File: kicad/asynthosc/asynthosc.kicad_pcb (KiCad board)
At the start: 4 copper layers, 71.5 x 128.5 mm, 201 parts, among them J1 USB_B_Micro, J11 Conn_01x04_Pin, J13 AudioJack3, J14 AudioJack3, J15 AudioJack3, J16 AudioJack3, J2 Conn_02x05_Odd_Even, J4 AudioJack3, J5 AudioJack3, J6 Conn_01x04_Pin, J7 AudioJack3, J9 Conn_01x07_Pin, Q2 Q_NPN_BEC, SW4 SW_MEC_5G_LED, SW7 SW_MEC_5G_LED, U1 LM1117S-3.3, U10 W25Q32JVSS, U11 LM1117S-5.0, U12 Si1869DH, U2 STM32H723ZGTx, U3 MCP6004, U4 MCP6004, U5 LAN8742A, U6 USBLC6-2P6, U7 USBLC6-2SC6, U8 H11L1, U9 LMR62421XMF, Y1 8MHz, 8pF, Y2 25MHZ,20PF,30PPM

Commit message: wip
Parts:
- removed the J13 at (103.5, 82.0)
- removed the J13 at (115.0, 82.0)
- removed the J13 at (126.5, 106.0)
- removed the J13 at (138.0, 106.0)
- removed the J13 at (115.0, 106.0)
- removed J6: Conn_01x04_Pin, Connector_PinHeader_2.54mm:PinHeader_1x04_P2.54mm_Vertical
- removed the SW4 at (116.5, 70.5)
- removed the SW4 at (107.5, 70.5)
- removed the SW4 at (134.5, 70.5)
- removed the SW4 at (138.0, 96.0)
- removed the SW4 at (114.5, 96.0)
- removed the SW4 at (126.5, 96.0)
- removed the SW4 at (125.5, 70.5)
- added C46: 10u, Capacitor_SMD:CP_Elec_4x5.4, F.Cu at (267.4, 47.4)
- added C55: 100n, Capacitor_SMD:C_0402_1005Metric, F.Cu at (258.7, 48.3)
- added C56: 100n, Capacitor_SMD:C_0402_1005Metric, F.Cu at (258.7, 50.2)
- added C57: 100n, Capacitor_SMD:C_0603_1608Metric, F.Cu at (227.2, 110.5)
- added F1: Fuse, 1.25A, trip 2.5A, Resistor_SMD:R_0805_2012Metric, F.Cu at (265.7, 51.8)
- added FB1: BLM15PX330SN1D, Inductor_SMD:L_0402_1005Metric, F.Cu at (269.4, 51.3)
- added FB2: BLM15PX330SN1D, Inductor_SMD:L_0402_1005Metric, F.Cu at (265.0, 41.5)
- added FB3: BLM15PX330SN1D, Inductor_SMD:L_0402_1005Metric, F.Cu at (265.0, 56.3)
- added J10: Conn_02x07_Odd_Even, Connector_PinSocket_2.54mm:PinSocket_2x07_P2.54mm_Vertical_SMD, B.Cu at (121.0, 138.1)
- added J12: Conn_02x04_Odd_Even, Connector_PinHeader_2.54mm:PinHeader_2x04_P2.54mm_Vertical_SMD, B.Cu at (140.5, 142.2)
- added J3: RJ45_LED_Shielded, asynthosc:RJ45_HCTL_HC-RJ45-053-2, F.Cu at (139.4, 51.8)
- added J8: AudioJack3, asynthosc:Jack_3.5mm_3legs_XKB_PJ-3411_Vertical, F.Cu at (104.5, 84.7)
- added J9: Conn_ARM_SWD_TagConnect_TC2030-NL, Connector:Tag-Connect_TC2030-IDC-NL_2x03_P1.27mm_Vertical, F.Cu at (151.0, 147.5)
- added Q1: Q_NPN_BEC, Package_TO_SOT_SMD:SOT-23, F.Cu at (242.6, 107.5)
- added R75: 10k, Resistor_SMD:R_0402_1005Metric, F.Cu at (255.8, 48.3)
- added R77: 10k, Resistor_SMD:R_0402_1005Metric, F.Cu at (255.8, 50.3)
- added R78: 10k, Resistor_SMD:R_0402_1005Metric, F.Cu at (255.8, 52.2)
- added R79: 270R, Resistor_SMD:R_0402_1005Metric, F.Cu at (255.8, 54.2)
- added R80: 100k, Resistor_SMD:R_0402_1005Metric, F.Cu at (238.7, 106.1)
- added R81: 10k, Resistor_SMD:R_0402_1005Metric, F.Cu at (238.7, 108.1)
- added R82: 270R, Resistor_SMD:R_0402_1005Metric, F.Cu at (238.7, 110.1)
- added REF**: LQFP-100_14x14mm_P0.5mm, Package_QFP:LQFP-100_14x14mm_P0.5mm, F.Cu at (145.0, 131.5)
- added SW10: SW_MEC_5G_LED, asynthosc:TPB01-X0XLXX_SW_MEC_5G, F.Cu at (136.0, 108.5)
- added SW2: SW_Push, Button_Switch_SMD:SW_SPST_B3S-1000, B.Cu at (97.2, 144.2)
- added SW3: RotaryEncoder, Rotary_Encoder:RotaryEncoder_Alps_EC12E_Vertical_H20mm, F.Cu at (118.0, 80.5)
- added SW9: SW_MEC_5G_LED, asynthosc:TPB01-X0XLXX_SW_MEC_5G, F.Cu at (134.0, 72.0)
- added TH1: Thermistor_NTC, Resistor_THT:R_Axial_DIN0204_L3.6mm_D1.6mm_P7.62mm_Horizontal, F.Cu at (168.0, 44.0)
- Q2: footprint Resistor_SMD:R_0402_1005Metric -> Package_TO_SOT_SMD:SOT-23
- moved D2 175.3 mm to (51.5, 43.6)
- moved U12 170.6 mm to (51.8, 49.7)
- moved U11 126.7 mm to (67.7, 47.6)
- moved J7 117.7 mm to (115.0, 86.8)
- moved Y1 106.7 mm to (106.5, 134.0)
- moved Y2 99.3 mm to (96.5, 121.5)
- moved J16 96.9 mm to (137.2, 97.0), turned to 90 degrees
- moved J14 94.6 mm to (104.0, 95.8), turned to -90 degrees
- moved U10 74.0 mm to (101.6, 142.6)
- moved SW7 71.3 mm to (107.5, 72.0)
- moved L1 59.6 mm to (88.0, 84.5)
- moved J15 55.0 mm to (125.8, 99.0)
- moved TR1 41.5 mm to (146.8, 67.2)
- moved U1 27.9 mm to (102.4, 60.5)
- moved R76 27.6 mm to (183.5, 43.5)
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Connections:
- R15 pad 1: Net-(J9-Pin_4) -> /Soc/JTMS_CONN
- R16 pad 1: Net-(J9-Pin_5) -> /Soc/NRST_CONN
- R17 pad 1: Net-(J9-Pin_6) -> /Soc/JTDO_CONN
- R20 pad 1: Net-(J11-Pin_1) -> Net-(J12-Pin_7)
- R7 pad 1: Net-(J9-Pin_7) -> /Soc/JTDI_CONN
- R8 pad 1: Net-(J9-Pin_2) -> /Soc/JTCK_CONN
- U2 pad 66: /Soc/TIM1_CH3 -> /Analog_in/TRG1
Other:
- board size 71.5 x 128.5 mm -> 69 x 106 mm
- board text added: "(OK)"
- board text added: "(cancel)"
- board text added: "13mm between boards"
- board text added: "71.12 mm = 14 x 5.08mm = 14 HP"
- board text added: "AUDIO OUT"
- board text added: "BTN"
- board text added: "CV"
- board text added: "DISPLAY"
- board text added: "JACK"
- board text added: "MIDI IN"
- board text added: "PANEL"
- board text added: "PCB"
- board text added: "ROT"
- board text added: "TRIG"

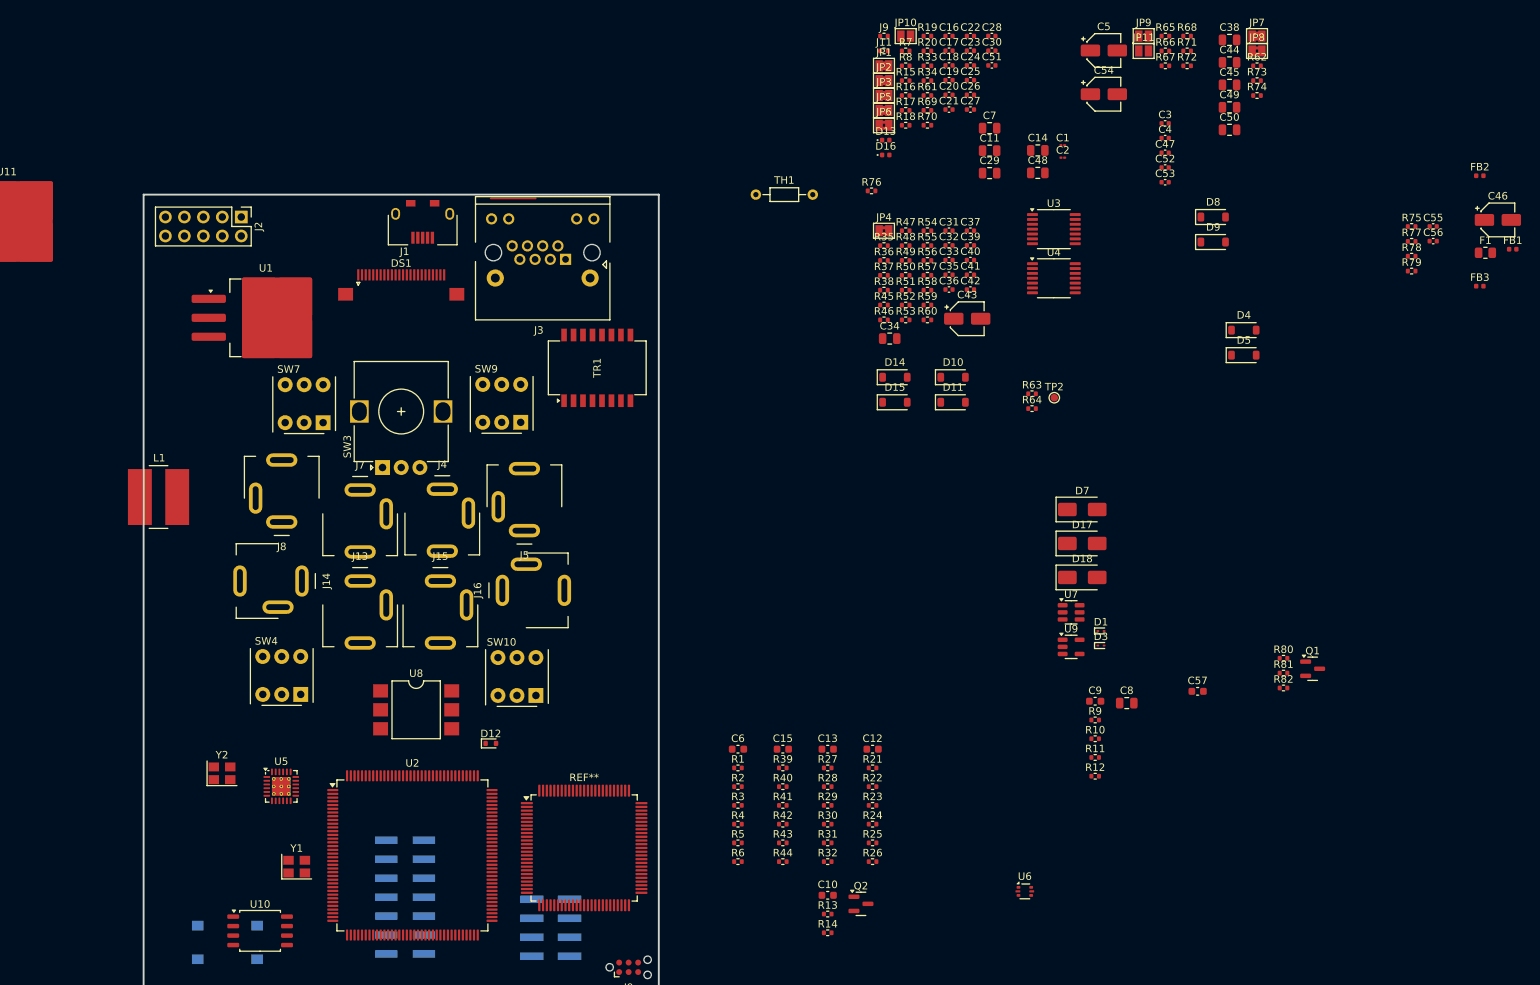
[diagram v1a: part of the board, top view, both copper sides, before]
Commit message: sch: change stm32 for smaller one, create smaller jumper footprint
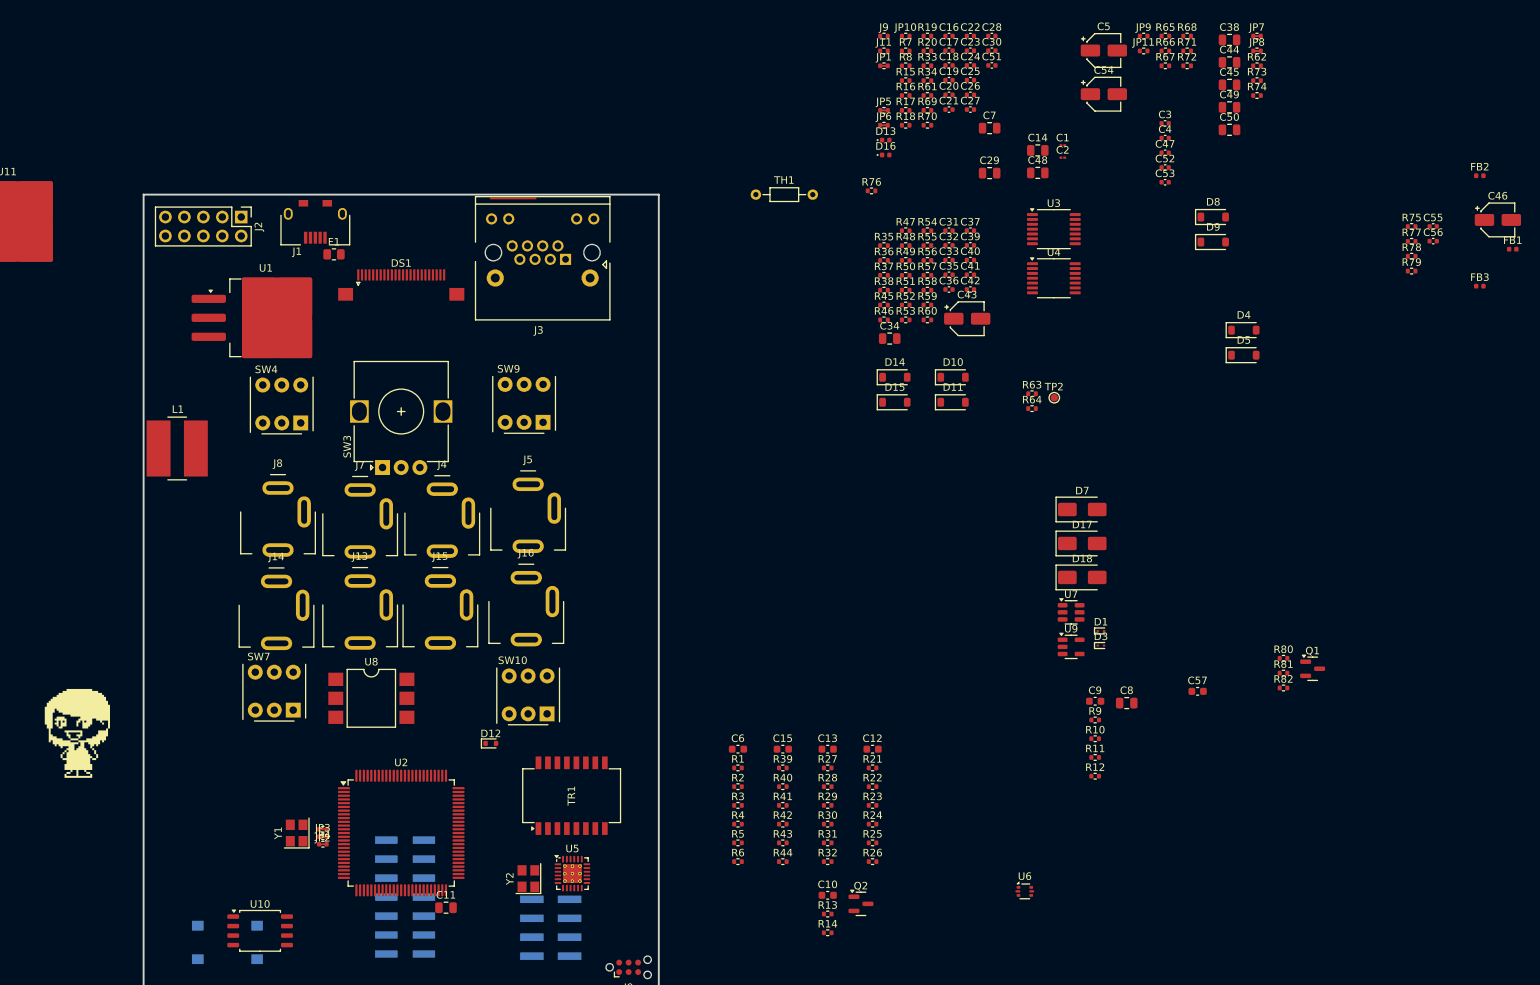
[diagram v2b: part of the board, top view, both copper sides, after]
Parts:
- removed REF**: LQFP-100_14x14mm_P0.5mm, Package_QFP:LQFP-100_14x14mm_P0.5mm
- JP1, JP2, JP3, JP4, JP5, JP6, JP7, JP8: footprint Jumper:SolderJumper-2_P1.3mm_Bridged2Bar_Pad1.0x1.5mm -> asynthosc:SolderJumper_0402_1005Metric_Bridged
- JP10, JP11, JP9: footprint Jumper:SolderJumper-2_P1.3mm_Open_Pad1.0x1.5mm -> Resistor_SMD:R_0402_1005Metric
- U2: value STM32H723ZGTx -> STM32F723VETx; footprint Package_QFP:LQFP-144_20x20mm_P0.5mm -> Package_QFP:LQFP-100_14x14mm_P0.5mm
- moved F1 154.2 mm to (111.5, 52.0)
- moved JP2 125.3 mm to (110.0, 129.0), turned to 180 degrees
- moved C11 124.8 mm to (126.5, 139.5)
- moved JP3 124.5 mm to (110.0, 130.0)
- moved JP4 111.3 mm to (110.0, 131.0)
- moved TR1 57.4 mm to (143.3, 124.5)
- moved Y2 43.4 mm to (137.5, 135.6), turned to 90 degrees
- moved U5 40.7 mm to (143.4, 134.9)
- moved SW7 38.7 mm to (103.5, 110.5)
- moved SW4 36.4 mm to (104.5, 72.0)
- moved J1 14.4 mm to (109.0, 49.8)
- moved L1 6.96 mm to (90.5, 78.0)
- moved U8 6.19 mm to (116.5, 111.5)
- moved Y1 4.50 mm to (106.5, 129.5), turned to 90 degrees
- moved U2 3.35 mm to (120.5, 129.5)
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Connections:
- net /Soc/TIM4_CH1 renamed /Soc/UART4_RX
- net /Soc/TIM4_CH2 renamed /Soc/UART4_TX
- C11 pad 1: Net-(C11-Pad1) -> Net-(U2-VCAP_1)
- C13 pad 1: /Soc/ADC1_IN3 -> /Analog_in/CVIN1
- C7 pad 1: Net-(C7-Pad1) -> Net-(U2-VCAP_2)
- D10 pad 2: /Soc/ADC1_IN3 -> /Analog_in/CVIN1
- D11 pad 1: /Soc/ADC1_IN3 -> /Analog_in/CVIN1
- R18 pad 2: /Soc/USART3_DBG_TX -> /Soc/USART3_BOOT_DBG_TX
- R19 pad 2: /Soc/USART3_DBG_RX -> /Soc/RMII_TX_EN
- R32 pad 1: /Soc/ADC1_IN3 -> /Analog_in/CVIN1
- U2 pad 1: /Interface/SCLK -> /Soc/QSPI_BK2_IO2
- U2 pad 10: unconnected-(U2-PF0-Pad10) -> GND
- U2 pad 100: /Soc/USB_SOF -> 3V3
- U2 pad 11: unconnected-(U2-PF1-Pad11) -> 3V3
- U2 pad 12: unconnected-(U2-PF2-Pad12) -> Net-(JP2-A)
- U2 pad 13: unconnected-(U2-PF3-Pad13) -> Net-(JP3-A)
- U2 pad 14: unconnected-(U2-PF4-Pad14) -> /Soc/NRST
- U2 pad 15: unconnected-(U2-PF5-Pad15) -> /Soc/ADC1_IN9
- U2 pad 16: GND -> /Soc/RMII_MDC
- U2 pad 17: 3V3 -> unconnected-(U2-PC2-Pad17)
- U2 pad 18: unconnected-(U2-PF6-Pad18) -> /Soc/QSPI_BK2_IO0
- U2 pad 19: /Soc/SPI5_SCK -> GND
- U2 pad 20: /Soc/SPI5_MISO -> /Soc/VDDA
- U2 pad 21: unconnected-(U2-PF9-Pad21) -> /Soc/VDDA
- U2 pad 22: unconnected-(U2-PF10-Pad22) -> /Analog_in/CVIN0
- U2 pad 23: Net-(JP2-A) -> /Soc/RMII_REF_CLK
- U2 pad 24: Net-(JP3-A) -> /Soc/RMII_MDIO
- U2 pad 25: /Soc/NRST -> /Analog_in/CVIN1
- U2 pad 26: /Soc/ADC1_IN10 -> GND
- U2 pad 27: /Soc/RMII_MDC -> 3V3
- U2 pad 28: /Soc/ADC1_IN12 -> /Soc/DAC_OUT1
- U2 pad 29: /Soc/ADC1_IN13 -> /Analog_in/CVIN2
- U2 pad 30: 3V3 -> /Analog_in/CVIN3
- U2 pad 31: GND -> /Soc/RMII_CRS_DV
- U2 pad 32: /Soc/VDDA -> /Soc/RMII_RXD0
- U2 pad 33: /Soc/VDDA -> /Soc/RMII_RXD1
- U2 pad 34: /Analog_in/CVIN0 -> /Soc/QSPI_BK2_IO1
- U2 pad 35: /Soc/RMII_REF_CLK -> /Soc/ADC1_IN8
- U2 pad 36: /Soc/RMII_MDIO -> /Soc/QSPI_CLK
- U2 pad 37: /Soc/ADC1_IN3 -> unconnected-(U2-PE7-Pad37)
- U2 pad 38: GND -> unconnected-(U2-PE8-Pad38)
- U2 pad 39: 3V3 -> /Soc/TIM1_CH1
- U2 pad 4: /Soc/SPI4_MISO -> /Soc/TIM15_CH1
- U2 pad 40: /Soc/DAC_OUT1 -> unconnected-(U2-PE10-Pad40)
- U2 pad 41: /Analog_in/CVIN2 -> /Soc/QSPI_BK2_NCS
- U2 pad 42: /Analog_in/CVIN3 -> unconnected-(U2-PE12-Pad42)
- U2 pad 43: /Soc/RMII_CRS_DV -> /Analog_in/TRG1
- U2 pad 44: /Soc/RMII_RXD0 -> unconnected-(U2-PE14-Pad44)
- U2 pad 45: /Soc/RMII_RXD1 -> unconnected-(U2-PE15-Pad45)
- U2 pad 46: /Soc/ADC1_IN8 -> /Soc/USART3_BOOT_DBG_TX
- U2 pad 47: /Soc/ADC1_IN9 -> /Soc/RMII_TX_EN
- U2 pad 48: unconnected-(U2-PB2-Pad48) -> Net-(U2-VCAP_1)
- U2 pad 49: /Soc/SPI5_MOSI -> GND
- U2 pad 5: /Interface/SDIN -> /Soc/TIM15_CH2
- U2 pad 50: unconnected-(U2-PF12-Pad50) -> 3V3
- U2 pad 51: GND -> /Soc/RMII_TXD0
- U2 pad 52: 3V3 -> /Soc/RMII_TXD1
- U2 pad 58: /Soc/QSPI_BK2_IO0 -> unconnected-(U2-PD11-Pad58)
- U2 pad 59: /Soc/QSPI_BK2_IO1 -> unconnected-(U2-PD12-Pad59)
- U2 pad 60: /Soc/QSPI_BK2_IO2 -> /Soc/QSPI_BK2_IO3
- U2 pad 61: GND -> unconnected-(U2-PD14-Pad61)
- U2 pad 62: 3V3 -> unconnected-(U2-PD15-Pad62)
- U2 pad 63: /Soc/QSPI_BK2_IO3 -> unconnected-(U2-PC6-Pad63)
- U2 pad 64: /Analog_in/TRG0 -> unconnected-(U2-PC7-Pad64)
- U2 pad 66: /Analog_in/TRG1 -> unconnected-(U2-PC9-Pad66)
- U2 pad 67: /Soc/TIM1_CH4 -> unconnected-(U2-PA8-Pad67)
- U2 pad 68: unconnected-(U2-PE15-Pad68) -> Net-(U2-PA9)
- U2 pad 69: unconnected-(U2-PB10-Pad69) -> /Soc/USB_ID
- U2 pad 70: unconnected-(U2-PB11-Pad70) -> /Soc/USB_D_N
- U2 pad 71: Net-(C11-Pad1) -> /Soc/USB_D_P
- U2 pad 72: 3V3 -> /Soc/JTMS
- U2 pad 73: unconnected-(U2-PB12-Pad73) -> Net-(U2-VCAP_2)
- U2 pad 74: /Soc/RMII_TXD1 -> GND
- U2 pad 75: unconnected-(U2-PB14-Pad75) -> 3V3
- U2 pad 76: unconnected-(U2-PB15-Pad76) -> /Soc/JTCK
- U2 pad 77: /Soc/USART3_DBG_TX -> /Soc/JTDI
- U2 pad 78: /Soc/USART3_DBG_RX -> /Interface/SCLK
- U2 pad 79: unconnected-(U2-PD10-Pad79) -> /Soc/SPI4_MISO
- U2 pad 80: unconnected-(U2-PD11-Pad80) -> /Interface/SDIN
- U2 pad 83: GND -> unconnected-(U2-PD2-Pad83)
- U2 pad 84: 3V3 -> unconnected-(U2-PD3-Pad84)
- U2 pad 85: /Soc/TIM4_CH3 -> unconnected-(U2-PD4-Pad85)
- U2 pad 86: /Soc/TIM4_CH4 -> /Soc/USART2_DBG_TX
- U2 pad 87: unconnected-(U2-PG2-Pad87) -> /Soc/USART2_DBG_RX
- U2 pad 89: unconnected-(U2-PG4-Pad89) -> /Soc/JTDO
- U2 pad 90: unconnected-(U2-PG5-Pad90) -> Net-(JP6-B)
- U2 pad 94: GND -> /Soc/BOOT0
- U2 pad 95: 3V3 -> unconnected-(U2-PB8-Pad95)
- U2 pad 99: unconnected-(U2-PC9-Pad99) -> GND
- U3 pad 7: /Soc/ADC1_IN3 -> /Analog_in/CVIN1
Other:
- board text added: "AsynthOsc V1"
- board text added: "RederoTech"
